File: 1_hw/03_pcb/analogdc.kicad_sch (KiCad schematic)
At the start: 12 parts, among them U24 LM6171, U25 TMUX6104

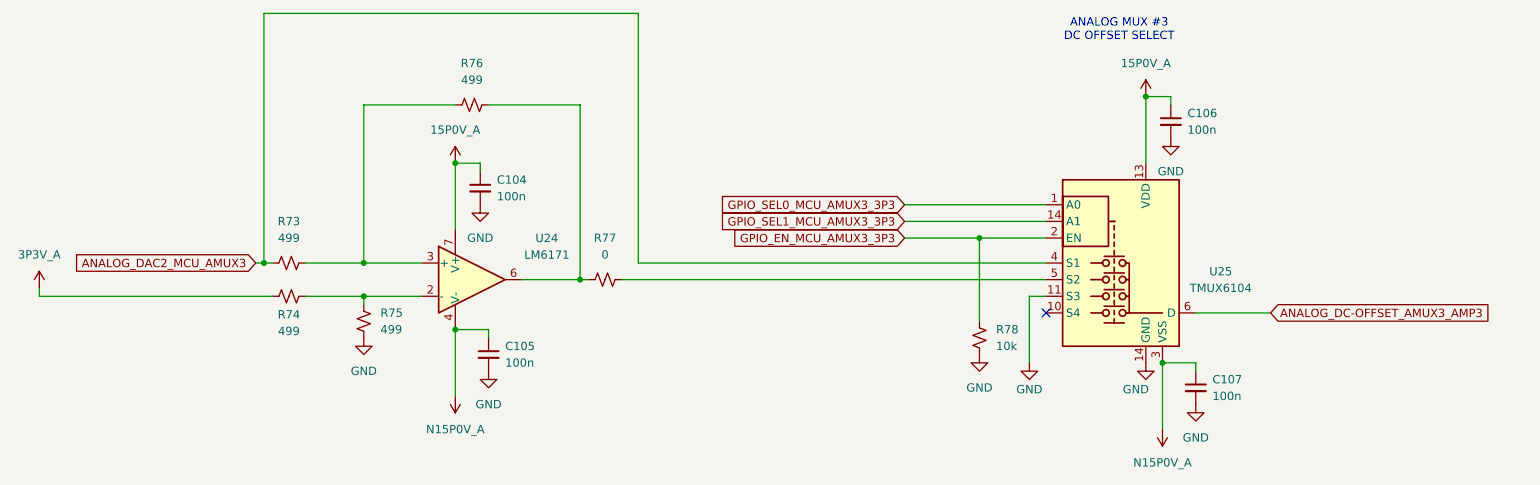
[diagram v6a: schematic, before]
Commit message: FEAT: Added MCU Flash. Finished creating & assigning footprints. Ran ERC & cleared out issues. Ready for Layout.
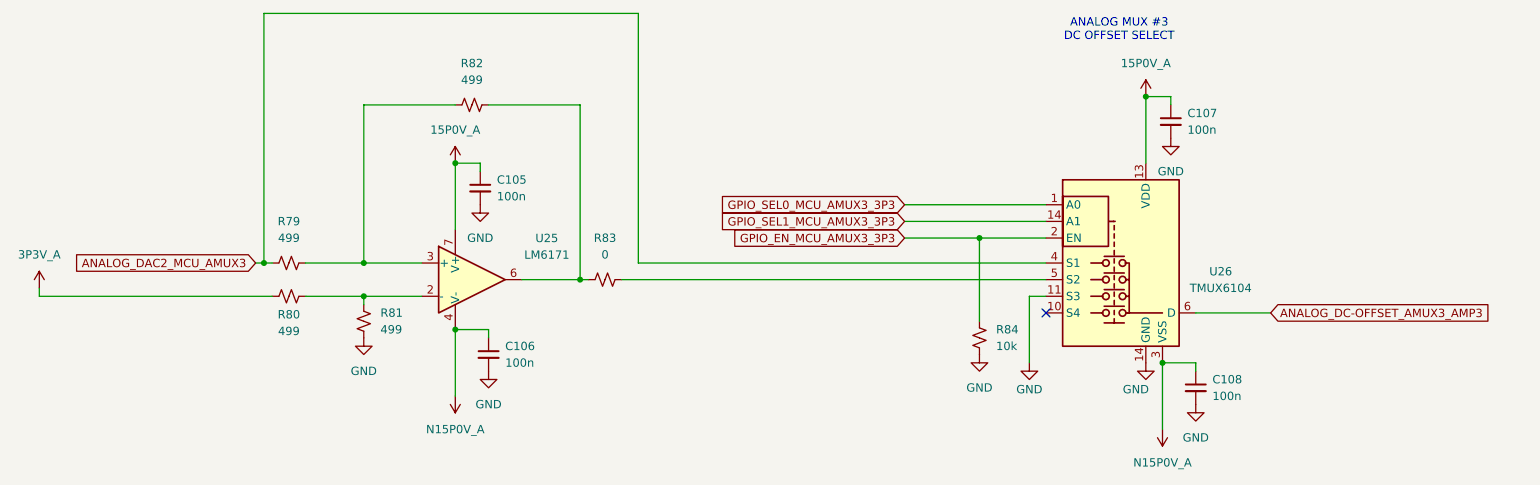
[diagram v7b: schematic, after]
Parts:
- U26: renamed from U25; footprint (none) -> Package_SO:TSSOP-14_4.4x5mm_P0.65mm
- renumbered C104 to C105, C105 to C106, C106 to C107, C107 to C108, R73 to R79, R74 to R80, R75 to R81, R76 to R82, R77 to R83, R78 to R84, U24 to U25
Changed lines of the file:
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@@
 		(dnp no)
 		(fields_autoplaced yes)
-		(property "Reference" "R78"
+		(property "Reference" "R84"
 			(at 186.69 110.4899 0)
 			(effects
@@
 			(project "arb"
 				(path "/866ef9be-3b01-4288-a6e0-a2357aa17e50/dd20ed2c-105a-40ef-bdba-a4198899f68e"
-					(reference "R78")
+					(reference "R84")
 					(unit 1)
 				)
@@
 		(dnp no)
 		(fields_autoplaced yes)
-		(property "Reference" "C105"
+		(property "Reference" "C106"
 			(at 111.76 113.0363 0)
 			(effects
@@
 			(project "arb"
 				(path "/866ef9be-3b01-4288-a6e0-a2357aa17e50/dd20ed2c-105a-40ef-bdba-a4198899f68e"
-					(reference "C105")
+					(reference "C106")
 					(unit 1)
 				)
@@
 		(on_board yes)
 		(dnp no)
-		(property "Reference" "#PWR0259"
+		(property "Reference" "#PWR0274"
 			(at 209.55 121.92 0)
 			(effects
@@
 			(project "arb"
 				(path "/866ef9be-3b01-4288-a6e0-a2357aa17e50/dd20ed2c-105a-40ef-bdba-a4198899f68e"
-					(reference "#PWR0259")
+					(reference "#PWR0274")
 					(unit 1)
 				)
@@
 		(on_board yes)
 		(dnp no)
-		(property "Reference" "#PWR0257"
+		(property "Reference" "#PWR0272"
 			(at 191.77 121.92 0)
 			(effects
@@
 			(project "arb"
 				(path "/866ef9be-3b01-4288-a6e0-a2357aa17e50/dd20ed2c-105a-40ef-bdba-a4198899f68e"
-					(reference "#PWR0257")
+					(reference "#PWR0272")
 					(unit 1)
 				)
@@
 		(dnp no)
 		(fields_autoplaced yes)
-		(property "Reference" "R75"
+		(property "Reference" "R81"
 			(at 92.71 107.9499 0)
 			(effects
@@
 			(project "arb"
 				(path "/866ef9be-3b01-4288-a6e0-a2357aa17e50/dd20ed2c-105a-40ef-bdba-a4198899f68e"
-					(reference "R75")
+					(reference "R81")
 					(unit 1)
 				)
@@
 		(dnp no)
 		(fields_autoplaced yes)
-		(property "Reference" "#PWR0250"
+		(property "Reference" "#PWR0265"
 			(at 40.64 107.95 0)
 			(effects
@@
 			(project "arb"
 				(path "/866ef9be-3b01-4288-a6e0-a2357aa17e50/dd20ed2c-105a-40ef-bdba-a4198899f68e"
-					(reference "#PWR0250")
+					(reference "#PWR0265")
 					(unit 1)
 				)
@@
 		(dnp no)
 		(fields_autoplaced yes)
-		(property "Reference" "#PWR0261"
+		(property "Reference" "#PWR0276"
 			(at 213.36 87.63 0)
 			(effects
@@
 			(project "arb"
 				(path "/866ef9be-3b01-4288-a6e0-a2357aa17e50/dd20ed2c-105a-40ef-bdba-a4198899f68e"
-					(reference "#PWR0261")
+					(reference "#PWR0276")
 					(unit 1)
 				)
@@
 		(on_board yes)
 		(dnp no)
-		(property "Reference" "R74"
+		(property "Reference" "R80"
 			(at 78.74 108.204 90)
 			(effects
@@
 			(project "arb"
 				(path "/866ef9be-3b01-4288-a6e0-a2357aa17e50/dd20ed2c-105a-40ef-bdba-a4198899f68e"
-					(reference "R74")
+					(reference "R80")
 					(unit 1)
 				)
@@
 		(dnp no)
 		(fields_autoplaced yes)
-		(property "Reference" "R76"
+		(property "Reference" "R82"
 			(at 106.68 69.85 90)
 			(effects
@@
 			(project "arb"
 				(path "/866ef9be-3b01-4288-a6e0-a2357aa17e50/dd20ed2c-105a-40ef-bdba-a4198899f68e"
-					(reference "R76")
+					(reference "R82")
 					(unit 1)
 				)
@@
 		(dnp no)
 		(fields_autoplaced yes)
-		(property "Reference" "#PWR0251"
+		(property "Reference" "#PWR0266"
 			(at 90.17 118.11 0)
 			(effects
@@
 			(project "arb"
 				(path "/866ef9be-3b01-4288-a6e0-a2357aa17e50/dd20ed2c-105a-40ef-bdba-a4198899f68e"
-					(reference "#PWR0251")
+					(reference "#PWR0266")
 					(unit 1)
 				)
@@
 		(dnp no)
 		(fields_autoplaced yes)
-		(property "Reference" "#PWR0255"
+		(property "Reference" "#PWR0270"
 			(at 109.22 123.19 0)
 			(effects
@@
 			(project "arb"
 				(path "/866ef9be-3b01-4288-a6e0-a2357aa17e50/dd20ed2c-105a-40ef-bdba-a4198899f68e"
-					(reference "#PWR0255")
+					(reference "#PWR0270")
 					(unit 1)
 				)
@@
 		(dnp no)
 		(fields_autoplaced yes)
-		(property "Reference" "#PWR0253"
+		(property "Reference" "#PWR0268"
 			(at 104.14 116.84 0)
 			(effects
@@
 			(project "arb"
 				(path "/866ef9be-3b01-4288-a6e0-a2357aa17e50/dd20ed2c-105a-40ef-bdba-a4198899f68e"
-					(reference "#PWR0253")
+					(reference "#PWR0268")
 					(unit 1)
 				)
@@
 		(dnp no)
 		(fields_autoplaced yes)
-		(property "Reference" "#PWR0252"
+		(property "Reference" "#PWR0267"
 			(at 104.14 88.9 0)
 			(effects
@@
 			(project "arb"
 				(path "/866ef9be-3b01-4288-a6e0-a2357aa17e50/dd20ed2c-105a-40ef-bdba-a4198899f68e"
-					(reference "#PWR0252")
+					(reference "#PWR0267")
 					(unit 1)
 				)
@@
 		(dnp no)
 		(fields_autoplaced yes)
-		(property "Reference" "#PWR0256"
+		(property "Reference" "#PWR0271"
 			(at 184.15 120.65 0)
 			(effects
@@
 			(project "arb"
 				(path "/866ef9be-3b01-4288-a6e0-a2357aa17e50/dd20ed2c-105a-40ef-bdba-a4198899f68e"
-					(reference "#PWR0256")
+					(reference "#PWR0271")
 					(unit 1)
 				)
@@
 		(dnp no)
 		(fields_autoplaced yes)
-		(property "Reference" "R73"
+		(property "Reference" "R79"
 			(at 78.74 93.98 90)
 			(effects
@@
 			(project "arb"
 				(path "/866ef9be-3b01-4288-a6e0-a2357aa17e50/dd20ed2c-105a-40ef-bdba-a4198899f68e"
-					(reference "R73")
+					(reference "R79")
 					(unit 1)
 				)
@@
 		(dnp no)
 		(fields_autoplaced yes)
-		(property "Reference" "C107"
+		(property "Reference" "C108"
 			(at 219.71 118.1163 0)
 			(effects
@@
 			(project "arb"
 				(path "/866ef9be-3b01-4288-a6e0-a2357aa17e50/dd20ed2c-105a-40ef-bdba-a4198899f68e"
-					(reference "C107")
+					(reference "C108")
 					(unit 1)
 				)
@@
 		(dnp no)
 		(fields_autoplaced yes)
-		(property "Reference" "R77"
+		(property "Reference" "R83"
 			(at 127 96.52 90)
 			(effects
@@
 			(project "arb"
 				(path "/866ef9be-3b01-4288-a6e0-a2357aa17e50/dd20ed2c-105a-40ef-bdba-a4198899f68e"
-					(reference "R77")
+					(reference "R83")
 					(unit 1)
 				)
@@
 		(dnp no)
 		(fields_autoplaced yes)
-		(property "Reference" "#PWR0258"
+		(property "Reference" "#PWR0273"
 			(at 209.55 78.74 0)
 			(effects
@@
 			(project "arb"
 				(path "/866ef9be-3b01-4288-a6e0-a2357aa17e50/dd20ed2c-105a-40ef-bdba-a4198899f68e"
-					(reference "#PWR0258")
+					(reference "#PWR0273")
 					(unit 1)
 				)
@@
 		(dnp no)
 		(fields_autoplaced yes)
-		(property "Reference" "C106"
+		(property "Reference" "C107"
 			(at 215.9 77.4763 0)
 			(effects
@@
 			(project "arb"
 				(path "/866ef9be-3b01-4288-a6e0-a2357aa17e50/dd20ed2c-105a-40ef-bdba-a4198899f68e"
-					(reference "C106")
+					(reference "C107")
 					(unit 1)
 				)
@@
 		(dnp no)
 		(fields_autoplaced yes)
-		(property "Reference" "U24"
+		(property "Reference" "U25"
 			(at 118.11 96.5514 0)
 			(effects
@@
 			(project "arb"
 				(path "/866ef9be-3b01-4288-a6e0-a2357aa17e50/dd20ed2c-105a-40ef-bdba-a4198899f68e"
-					(reference "U24")
+					(reference "U25")
 					(unit 1)
 				)
@@
 		(dnp no)
 		(fields_autoplaced yes)
-		(property "Reference" "#PWR0260"
+		(property "Reference" "#PWR0275"
 			(at 212.09 121.92 0)
 			(effects
@@
 			(project "arb"
 				(path "/866ef9be-3b01-4288-a6e0-a2357aa17e50/dd20ed2c-105a-40ef-bdba-a4198899f68e"
-					(reference "#PWR0260")
+					(reference "#PWR0275")
 					(unit 1)
 				)
@@
 		(on_board yes)
 		(dnp no)
-		(property "Reference" "U25"
+		(property "Reference" "U26"
 			(at 220.98 101.6314 0)
 			(effects
@@
 			)
 		)
-		(property "Footprint" ""
+		(property "Footprint" "Package_SO:TSSOP-14_4.4x5mm_P0.65mm"
 			(at 204.47 105.41 0)
 			(effects
@@
 			(project "arb"
 				(path "/866ef9be-3b01-4288-a6e0-a2357aa17e50/dd20ed2c-105a-40ef-bdba-a4198899f68e"
-					(reference "U25")
+					(reference "U26")
 					(unit 1)
 				)
@@
 		(dnp no)
 		(fields_autoplaced yes)
-		(property "Reference" "#PWR0262"
+		(property "Reference" "#PWR0277"
 			(at 217.17 128.27 0)
 			(effects
@@
 			(project "arb"
 				(path "/866ef9be-3b01-4288-a6e0-a2357aa17e50/dd20ed2c-105a-40ef-bdba-a4198899f68e"
-					(reference "#PWR0262")
+					(reference "#PWR0277")
 					(unit 1)
 				)
@@
 		(dnp no)
 		(fields_autoplaced yes)
-		(property "Reference" "#PWR0254"
+		(property "Reference" "#PWR0269"
 			(at 107.95 97.79 0)
 			(effects
@@
 			(project "arb"
 				(path "/866ef9be-3b01-4288-a6e0-a2357aa17e50/dd20ed2c-105a-40ef-bdba-a4198899f68e"
-					(reference "#PWR0254")
+					(reference "#PWR0269")
 					(unit 1)
 				)
@@
 		(dnp no)
 		(fields_autoplaced yes)
-		(property "Reference" "C104"
+		(property "Reference" "C105"
 			(at 110.49 87.6363 0)
 			(effects
@@
 			(project "arb"
 				(path "/866ef9be-3b01-4288-a6e0-a2357aa17e50/dd20ed2c-105a-40ef-bdba-a4198899f68e"
-					(reference "C104")
-					(unit 1)
-				)
+					(reference "C105")
+					(unit 1)
+				)

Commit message: MINOR: Verified Footprints to Datasheets. Added Pull Ups on FPGA DONE/Config/SPI Chip Select Pins.
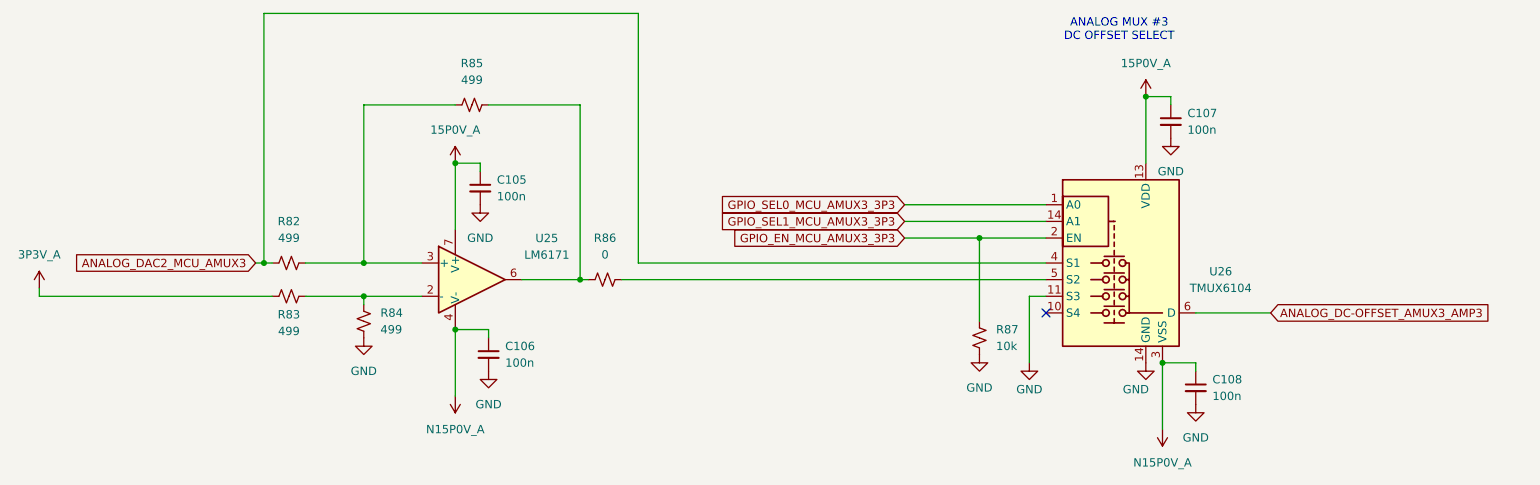
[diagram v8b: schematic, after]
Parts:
- renumbered R79 to R82, R80 to R83, R81 to R84, R82 to R85, R83 to R86, R84 to R87
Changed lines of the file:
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@@
 		(dnp no)
 		(fields_autoplaced yes)
-		(property "Reference" "R84"
+		(property "Reference" "R87"
 			(at 186.69 110.4899 0)
 			(effects
@@
 			(project "arb"
 				(path "/866ef9be-3b01-4288-a6e0-a2357aa17e50/dd20ed2c-105a-40ef-bdba-a4198899f68e"
-					(reference "R84")
+					(reference "R87")
 					(unit 1)
 				)
@@
 		(on_board yes)
 		(dnp no)
-		(property "Reference" "#PWR0274"
+		(property "Reference" "#PWR0277"
 			(at 209.55 121.92 0)
 			(effects
@@
 			(project "arb"
 				(path "/866ef9be-3b01-4288-a6e0-a2357aa17e50/dd20ed2c-105a-40ef-bdba-a4198899f68e"
-					(reference "#PWR0274")
+					(reference "#PWR0277")
 					(unit 1)
 				)
@@
 		(on_board yes)
 		(dnp no)
-		(property "Reference" "#PWR0272"
+		(property "Reference" "#PWR0275"
 			(at 191.77 121.92 0)
 			(effects
@@
 			(project "arb"
 				(path "/866ef9be-3b01-4288-a6e0-a2357aa17e50/dd20ed2c-105a-40ef-bdba-a4198899f68e"
-					(reference "#PWR0272")
+					(reference "#PWR0275")
 					(unit 1)
 				)
@@
 		(dnp no)
 		(fields_autoplaced yes)
-		(property "Reference" "R81"
+		(property "Reference" "R84"
 			(at 92.71 107.9499 0)
 			(effects
@@
 			(project "arb"
 				(path "/866ef9be-3b01-4288-a6e0-a2357aa17e50/dd20ed2c-105a-40ef-bdba-a4198899f68e"
-					(reference "R81")
+					(reference "R84")
 					(unit 1)
 				)
@@
 		(dnp no)
 		(fields_autoplaced yes)
-		(property "Reference" "#PWR0265"
+		(property "Reference" "#PWR0268"
 			(at 40.64 107.95 0)
 			(effects
@@
 			(project "arb"
 				(path "/866ef9be-3b01-4288-a6e0-a2357aa17e50/dd20ed2c-105a-40ef-bdba-a4198899f68e"
-					(reference "#PWR0265")
+					(reference "#PWR0268")
 					(unit 1)
 				)
@@
 		(dnp no)
 		(fields_autoplaced yes)
-		(property "Reference" "#PWR0276"
+		(property "Reference" "#PWR0279"
 			(at 213.36 87.63 0)
 			(effects
@@
 			(project "arb"
 				(path "/866ef9be-3b01-4288-a6e0-a2357aa17e50/dd20ed2c-105a-40ef-bdba-a4198899f68e"
-					(reference "#PWR0276")
+					(reference "#PWR0279")
 					(unit 1)
 				)
@@
 		(on_board yes)
 		(dnp no)
-		(property "Reference" "R80"
+		(property "Reference" "R83"
 			(at 78.74 108.204 90)
 			(effects
@@
 			(project "arb"
 				(path "/866ef9be-3b01-4288-a6e0-a2357aa17e50/dd20ed2c-105a-40ef-bdba-a4198899f68e"
-					(reference "R80")
+					(reference "R83")
 					(unit 1)
 				)
@@
 		(dnp no)
 		(fields_autoplaced yes)
-		(property "Reference" "R82"
+		(property "Reference" "R85"
 			(at 106.68 69.85 90)
 			(effects
@@
 			(project "arb"
 				(path "/866ef9be-3b01-4288-a6e0-a2357aa17e50/dd20ed2c-105a-40ef-bdba-a4198899f68e"
-					(reference "R82")
+					(reference "R85")
 					(unit 1)
 				)
@@
 		(dnp no)
 		(fields_autoplaced yes)
-		(property "Reference" "#PWR0266"
+		(property "Reference" "#PWR0269"
 			(at 90.17 118.11 0)
 			(effects
@@
 			(project "arb"
 				(path "/866ef9be-3b01-4288-a6e0-a2357aa17e50/dd20ed2c-105a-40ef-bdba-a4198899f68e"
-					(reference "#PWR0266")
+					(reference "#PWR0269")
 					(unit 1)
 				)
@@
 		(dnp no)
 		(fields_autoplaced yes)
-		(property "Reference" "#PWR0270"
+		(property "Reference" "#PWR0273"
 			(at 109.22 123.19 0)
 			(effects
@@
 			(project "arb"
 				(path "/866ef9be-3b01-4288-a6e0-a2357aa17e50/dd20ed2c-105a-40ef-bdba-a4198899f68e"
-					(reference "#PWR0270")
+					(reference "#PWR0273")
 					(unit 1)
 				)
@@
 		(dnp no)
 		(fields_autoplaced yes)
-		(property "Reference" "#PWR0268"
+		(property "Reference" "#PWR0271"
 			(at 104.14 116.84 0)
 			(effects
@@
 			(project "arb"
 				(path "/866ef9be-3b01-4288-a6e0-a2357aa17e50/dd20ed2c-105a-40ef-bdba-a4198899f68e"
-					(reference "#PWR0268")
+					(reference "#PWR0271")
 					(unit 1)
 				)
@@
 		(dnp no)
 		(fields_autoplaced yes)
-		(property "Reference" "#PWR0267"
+		(property "Reference" "#PWR0270"
 			(at 104.14 88.9 0)
 			(effects
@@
 			(project "arb"
 				(path "/866ef9be-3b01-4288-a6e0-a2357aa17e50/dd20ed2c-105a-40ef-bdba-a4198899f68e"
-					(reference "#PWR0267")
+					(reference "#PWR0270")
 					(unit 1)
 				)
@@
 		(dnp no)
 		(fields_autoplaced yes)
-		(property "Reference" "#PWR0271"
+		(property "Reference" "#PWR0274"
 			(at 184.15 120.65 0)
 			(effects
@@
 			(project "arb"
 				(path "/866ef9be-3b01-4288-a6e0-a2357aa17e50/dd20ed2c-105a-40ef-bdba-a4198899f68e"
-					(reference "#PWR0271")
+					(reference "#PWR0274")
 					(unit 1)
 				)
@@
 		(dnp no)
 		(fields_autoplaced yes)
-		(property "Reference" "R79"
+		(property "Reference" "R82"
 			(at 78.74 93.98 90)
 			(effects
@@
 			(project "arb"
 				(path "/866ef9be-3b01-4288-a6e0-a2357aa17e50/dd20ed2c-105a-40ef-bdba-a4198899f68e"
-					(reference "R79")
+					(reference "R82")
 					(unit 1)
 				)
@@
 		(dnp no)
 		(fields_autoplaced yes)
-		(property "Reference" "R83"
+		(property "Reference" "R86"
 			(at 127 96.52 90)
 			(effects
@@
 			(project "arb"
 				(path "/866ef9be-3b01-4288-a6e0-a2357aa17e50/dd20ed2c-105a-40ef-bdba-a4198899f68e"
-					(reference "R83")
+					(reference "R86")
 					(unit 1)
 				)
@@
 		(dnp no)
 		(fields_autoplaced yes)
-		(property "Reference" "#PWR0273"
+		(property "Reference" "#PWR0276"
 			(at 209.55 78.74 0)
 			(effects
@@
 			(project "arb"
 				(path "/866ef9be-3b01-4288-a6e0-a2357aa17e50/dd20ed2c-105a-40ef-bdba-a4198899f68e"
-					(reference "#PWR0273")
+					(reference "#PWR0276")
 					(unit 1)
 				)
@@
 		(dnp no)
 		(fields_autoplaced yes)
-		(property "Reference" "#PWR0275"
+		(property "Reference" "#PWR0278"
 			(at 212.09 121.92 0)
 			(effects
@@
 			(project "arb"
 				(path "/866ef9be-3b01-4288-a6e0-a2357aa17e50/dd20ed2c-105a-40ef-bdba-a4198899f68e"
-					(reference "#PWR0275")
+					(reference "#PWR0278")
 					(unit 1)
 				)
@@
 		(dnp no)
 		(fields_autoplaced yes)
-		(property "Reference" "#PWR0277"
+		(property "Reference" "#PWR0280"
 			(at 217.17 128.27 0)
 			(effects
@@
 			(project "arb"
 				(path "/866ef9be-3b01-4288-a6e0-a2357aa17e50/dd20ed2c-105a-40ef-bdba-a4198899f68e"
-					(reference "#PWR0277")
+					(reference "#PWR0280")
 					(unit 1)
 				)
@@
 		(dnp no)
 		(fields_autoplaced yes)
-		(property "Reference" "#PWR0269"
+		(property "Reference" "#PWR0272"
 			(at 107.95 97.79 0)
 			(effects
@@
 			(project "arb"
 				(path "/866ef9be-3b01-4288-a6e0-a2357aa17e50/dd20ed2c-105a-40ef-bdba-a4198899f68e"
-					(reference "#PWR0269")
-					(unit 1)
-				)
+					(reference "#PWR0272")
+					(unit 1)
+				)
